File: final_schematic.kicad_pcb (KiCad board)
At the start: 2 copper layers, 54.7 x 60.6 mm, 52 parts, among them J1 Battery Babysitter, J2 BB_SYSOFF, J3 BOOT0, J4 OLED Qwiic, J5 Prog, J8 GPS_COAX, SW1 SW_Push_SESS, SW2 SW_Push_RADIO, SW3 SW_Push_RST, U1 STM32L476VGTx, U2 MTK3339, U3 RFM95W-868S2, U4 BNO055, U5 LT1129-3.3_SO8

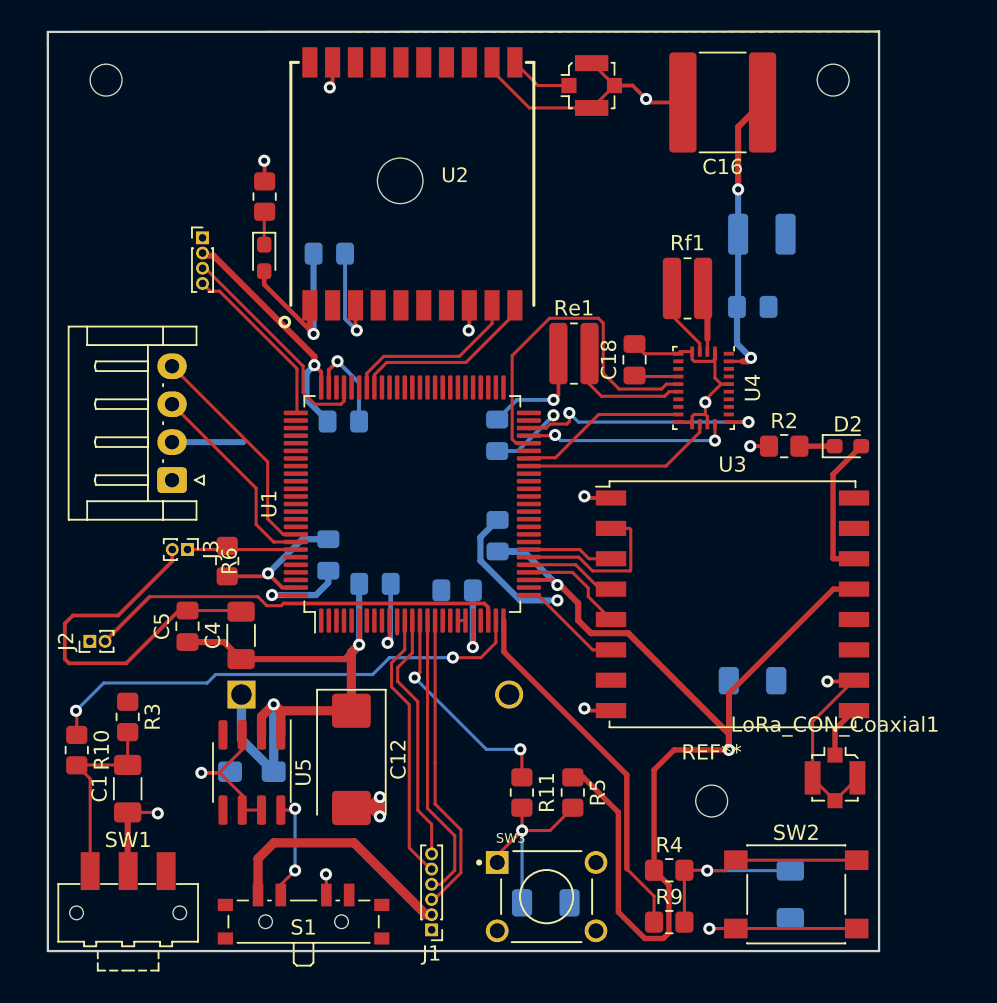
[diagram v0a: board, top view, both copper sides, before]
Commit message: Design Rules Pass, more silkskin
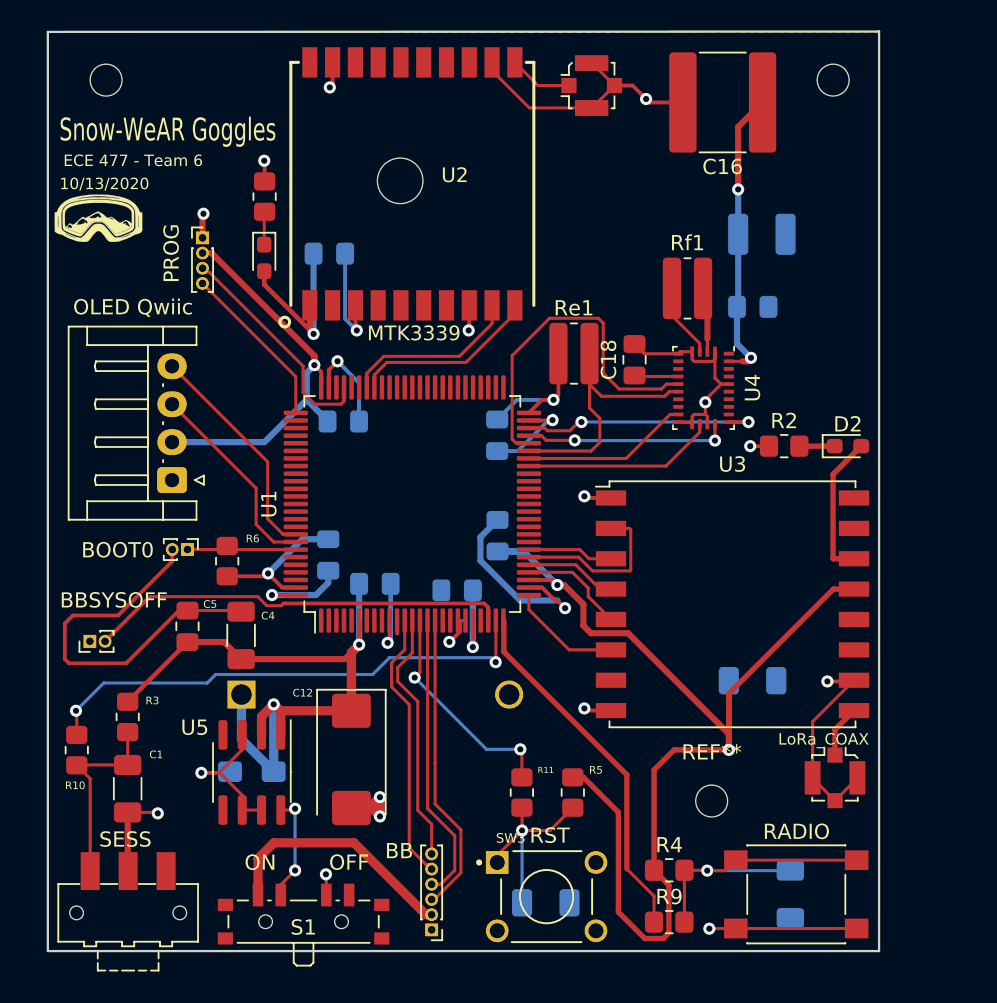
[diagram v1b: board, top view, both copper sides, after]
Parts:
- added G***: LOGO, footprint_lib:logo2, F.Cu at (100.6, 57.7)
- J2: value BB_SYSOFF -> BBSYSOFF
- J5: value Prog -> PROG
- REF**: value MountingHole_2.1mm -> 2.1mm
- renumbered J1 to BB, LoRa_CON_Coaxial1 to LoRa_COAX, SW2 to RADIO, SW1 to SESS
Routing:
- net 3V3: track 201.1 -> 215.1 mm
- net IMU_nRST: track 8.32 -> 19.4 mm
- net GND: track 158.9 -> 166.8 mm, vias 21 -> 23
- net LoRa_RST: track 6.90 -> 8.06 mm
- net session_btn: track 32.6 -> 33.6 mm
- net I2C2_SDA: track 16.8 -> 16.1 mm
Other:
- board text added: "10/13/2020"
- board text added: "BB_CE"
- board text added: "BB_GPOUT"
- board text added: "ECE 477 - Team 6"
- board text added: "I2C3_SCL"
- board text added: "I2C3_SDA"
- board text added: "OFF"
- board text added: "ON"
- board text added: "RST"
- board text added: "Snow-WeAR Goggles"
- board text added: "V_supply"

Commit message: Silkscreen is milkscreen
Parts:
- moved G*** 12.1 mm to (108.2, 48.3)
- renumbered U4 to BNO055, D1 to HEART, U3 to RADIO, D2 to TRANS
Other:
- board text added: "+"
- board text added: "-"
- board text added: "3V3"
- board text added: "BOOT0"
- board text added: "Brought to you by, Mitchell Ciupak Carrie Kemmet Kennedy Monaco Peter Sumner"
- board text added: "C3-PAD2"
- board text added: "GND"
- board text added: "GPS_COAX"
- board text added: "I2C1_SCL"
- board text added: "I2C1_SDA"
- board text added: "Icon Legend"
- board text added: "Pin 1"
- board text added: "SWCLK"
- board text added: "SWDIO"
- board text added: "SYSOFF"

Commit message: Cha Cha Cha Changes
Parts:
- removed C4: 1uF, Capacitor_SMD:C_1206_3216Metric_Pad1.33x1.80mm_HandSolder
- removed C5: 0.1uF, Capacitor_SMD:C_0805_2012Metric_Pad1.18x1.45mm_HandSolder
- removed J3: BOOT0, Connector_PinHeader_1.00mm:PinHeader_1x02_P1.00mm_Vertical
- removed R6: 510, Resistor_SMD:R_0805_2012Metric_Pad1.20x1.40mm_HandSolder
- D1: renamed from HEART; value HEART -> LED_HEARTBEAT_R1
- J1: renamed from BB; footprint Connector_PinHeader_1.00mm:PinHeader_1x06_P1.00mm_Vertical -> Connector_PinHeader_2.54mm:PinHeader_1x06_P2.54mm_Vertical
- J2: value BBSYSOFF -> BB_SYSOFF; footprint Connector_PinHeader_1.00mm:PinHeader_1x02_P1.00mm_Vertical -> Connector_PinHeader_2.54mm:PinHeader_1x02_P2.54mm_Vertical
- J5: value PROG -> Programmer; footprint Connector_PinHeader_1.00mm:PinHeader_1x04_P1.00mm_Vertical -> Connector_PinHeader_2.54mm:PinHeader_1x04_P2.54mm_Vertical
- moved J2 6.98 mm to (107.0, 84.9)
- moved J5 2.32 mm to (108.4, 61.1), turned to 270 degrees
- moved J1 0.61 mm to (122.5, 103.9)
- renumbered TRANS to D2, LoRa_COAX to LoRa_CON_Coaxial1, SESS to SW1, RADIO to SW2, RADIO to U3, BNO055 to U4
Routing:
- net GND: track 166.8 -> 145.9 mm, vias 23 -> 26
- net 3V3: track 215.1 -> 198.6 mm
- net SYSOFF: track 27.7 -> 18.5 mm
- net BB_CE: track 16.7 -> 8.38 mm
- net SWCLK: track 11.1 -> 18.5 mm
- net BOOT0: track 7.37 -> 0.00 mm
- net BB_GPOUT: track 17.9 -> 11.2 mm
- net I2C3_SCL: track 19.1 -> 13.2 mm
- net I2C3_SDA: track 20.0 -> 15.9 mm
- net SWDIO: track 15.3 -> 19.2 mm

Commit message: component update
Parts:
- added R12: 10k, Resistor_SMD:R_0805_2012Metric_Pad1.20x1.40mm_HandSolder, F.Cu at (109.3, 71.9)
- added R13: 10k, Resistor_SMD:R_0805_2012Metric_Pad1.20x1.40mm_HandSolder, B.Cu at (133.9, 69.7)
- added R14: 10k, Resistor_SMD:R_0805_2012Metric_Pad1.20x1.40mm_HandSolder, F.Cu at (126.6, 96.0)
- added R6: 10k, Resistor_SMD:R_0805_2012Metric_Pad1.20x1.40mm_HandSolder, F.Cu at (109.3, 69.8)
- added R7: 10k, Resistor_SMD:R_0805_2012Metric_Pad1.20x1.40mm_HandSolder, B.Cu at (136.1, 72.8)
- added R8: 10k, Resistor_SMD:R_0805_2012Metric_Pad1.20x1.40mm_HandSolder, F.Cu at (126.6, 93.4)
- added U6: TC2014-3.3VxCTTR, Package_TO_SOT_SMD:SOT-23-5, B.Cu at (122.3, 72.0)
- J5: footprint Connector_PinHeader_2.54mm:PinHeader_1x04_P2.54mm_Vertical -> Connector_PinHeader_2.54mm:PinHeader_1x05_P2.54mm_Vertical
- moved R9 4.97 mm to (135.9, 99.6), turned to 270 degrees
- moved R11 3.11 mm to (131.3, 96.8)
- moved D1 2.46 mm to (111.2, 57.8)
- moved R5 2.07 mm to (133.4, 96.8)
- moved J5 1.90 mm to (110.2, 61.6)
- moved R1 1.88 mm to (111.2, 54.4), turned to 0 degrees
- moved R4 1.02 mm to (138.1, 99.6), turned to 270 degrees
- moved J4 0.97 mm to (105.4, 75.8)
- moved G*** 0.91 mm to (107.2, 48.3)
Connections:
- C13 pad 1: 3V3 -> GPS_Vin
- J5 pad 2: 3V3 -> NRST
- J5 pad 3: SWDIO -> 3V3
- J5 pad 4: SWCLK -> SWDIO
- U1 pad 21: 3V3 -> GND
- U1 pad 22: Net-(U1-Pad22) -> 3V3
- U1 pad 64: Net-(U1-Pad64) -> LDO_ERR
- U1 pad 65: Net-(U1-Pad65) -> LDO_SHDN
- U1 pad 73: Net-(U1-Pad73) -> 3V3
- U1 pad 94: BOOT0 -> GND
- U2 pad 1: 3V3 -> GPS_Vin
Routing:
- net 3V3: track 198.6 -> 370.4 mm, vias 11 -> 13
- net NRST: track 14.6 -> 65.2 mm, vias 2 -> 3
- net LDO_ERR: track 0.00 -> 17.5 mm, vias 0 -> 1
- net GPS_Vin: track 0.00 -> 16.4 mm, vias 0 -> 1
- net GND: track 145.9 -> 158.4 mm
- net LDO_SHDN: track 0.00 -> 9.19 mm, vias 0 -> 1
- net radio_btn: track 24.0 -> 18.0 mm
- net I2C3_SDA: track 15.9 -> 18.6 mm
- net I2C3_SCL: track 13.2 -> 15.0 mm
- net USART_TX: track 12.3 -> 13.6 mm
- net SWCLK: track 18.5 -> 17.2 mm
- net Net-(D1-Pad1): track 2.17 -> 3.00 mm
- net SWDIO: track 19.2 -> 18.6 mm
- net Net-(C3-Pad2): track 12.5 -> 12.0 mm

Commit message: keepout
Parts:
- moved C13 3.57 mm to (115.8, 63.5)
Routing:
- net GND: track 158.4 -> 150.0 mm, vias 26 -> 27
- net GPS_Vin: track 16.4 -> 12.9 mm
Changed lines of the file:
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@@
     (thickness 1.6)
     (drawings 53)
-    (tracks 608)
+    (tracks 612)
     (zones 0)
     (modules 56)
@@
   )
   (module Capacitor_SMD:C_0805_2012Metric_Pad1.18x1.45mm_HandSolder (layer B.Cu)
-    (at 115.7947 59.9694)
+    (at 115.7732 63.5381)
     (descr "Capacitor SMD 0805 (2012 Metric), square (rectangular) end terminal, IPC_7351 nominal with elongated pad for handsoldering. (Body size source: IPC-SM-782 page 76, https://www.pcb-3d.com/wordpress/wp-content/uploads/ipc-sm-782a_amendment_1_and_2.pdf, https://docs.google.com/spreadsheets/d/1BsfQQcO9C6DZCsRaXUlFlo91Tg2WpOkGARC1WS5S8t0/edit?usp=sharing), generated with kicad-footprint-generator")
     (tags "capacitor handsolder")
@@
   (segment (start 133.0706 50.372001) (end 133.0956 50.372001) (width 0.2032) (layer F.Cu) (net 2))
   (segment (start 126.5096 47.914882) (end 126.5096 47.372) (width 0.2032) (layer F.Cu) (net 2))
-  (segment (start 128.966719 50.372001) (end 126.5096 47.914882) (width 0.2032) (layer F.Cu) (net 2))
-  (segment (start 133.0706 50.372001) (end 128.966719 50.372001) (width 0.2032) (layer F.Cu) (net 2))
   (segment (start 150.5216 104.4088) (end 142.5616 104.4088) (width 0.2032) (layer F.Cu) (net 2))
   (segment (start 147.6166 94.513) (end 149.0916 95.988) (width 0.2032) (layer F.Cu) (net 2))
@@
   (via (at 117.602 65.024) (size 0.8) (drill 0.4) (layers F.Cu B.Cu) (net 2))
   (segment (start 116.8322 64.2542) (end 117.602 65.024) (width 0.254) (layer B.Cu) (net 2))
-  (segment (start 116.8322 59.9694) (end 116.8322 64.2542) (width 0.254) (layer B.Cu) (net 2))
   (segment (start 117.5096 64.9316) (end 117.602 65.024) (width 0.254) (layer F.Cu) (net 2))
   (segment (start 117.5096 63.372) (end 117.5096 64.9316) (width 0.254) (layer F.Cu) (net 2))
@@
   (segment (start 125.2596 84.773) (end 124.4346 85.598) (width 0.254) (layer F.Cu) (net 2))
   (segment (start 125.2596 84.129) (end 125.2596 84.773) (width 0.254) (layer F.Cu) (net 2))
+  (via (at 126.492 48.9966) (size 0.8) (drill 0.4) (layers F.Cu B.Cu) (net 2))
+  (segment (start 126.5096 48.979) (end 126.492 48.9966) (width 0.254) (layer F.Cu) (net 2))
+  (segment (start 126.5096 47.372) (end 126.5096 48.979) (width 0.254) (layer F.Cu) (net 2))
+  (segment (start 116.8107 64.2327) (end 117.602 65.024) (width 0.254) (layer B.Cu) (net 2))
+  (segment (start 116.8107 63.5381) (end 116.8107 64.2327) (width 0.254) (layer B.Cu) (net 2))
   (via (at 107.0356 73.3298) (size 0.8) (drill 0.4) (layers F.Cu B.Cu) (net 5))
   (via (at 120.2055 66.9163) (size 0.8) (drill 0.4) (layers F.Cu B.Cu) (net 128))
@@
   (segment (start 112.5526 90.0688) (end 112.1307 89.6469) (width 0.6096) (layer F.Cu) (net 5))
   (segment (start 117.2464 90.0688) (end 112.5526 90.0688) (width 0.6096) (layer F.Cu) (net 5))
-  (segment (start 114.7572 59.9694) (end 114.7572 65.2526) (width 0.4064) (layer B.Cu) (net 126))
   (segment (start 114.7572 65.2526) (end 114.7572 65.2526) (width 0.4064) (layer B.Cu) (net 126))
   (via (at 114.7572 65.2526) (size 0.8) (drill 0.4) (layers F.Cu B.Cu) (net 126))
@@
   (segment (start 121.1756 70.4546) (end 115.9736 65.2526) (width 0.254) (layer B.Cu) (net 126))
   (segment (start 121.1756 71.0336) (end 121.1756 70.4546) (width 0.254) (layer B.Cu) (net 126))
+  (segment (start 114.7484 65.2438) (end 114.7572 65.2526) (width 0.254) (layer B.Cu) (net 126))
+  (segment (start 114.7357 65.2311) (end 114.7572 65.2526) (width 0.254) (layer B.Cu) (net 126))
+  (segment (start 114.7357 63.5381) (end 114.7357 65.2311) (width 0.254) (layer B.Cu) (net 126))
   (segment (start 120.7596 68.779) (end 120.7596 67.73077) (width 0.2032) (layer F.Cu) (net 127))
   (segment (start 121.77699 66.929) (end 122.301 66.929) (width 0.2032) (layer F.Cu) (net 127))
@@
       )
     )
+  )
+  (zone (net 0) (net_name "") (layer B.Cu) (hatch edge 0.508)
+    (connect_pads (clearance 0.508))
+    (min_thickness 0.254)
+    (keepout (tracks not_allowed) (vias not_allowed) (copperpour not_allowed))
+    (fill (arc_segments 32) (thermal_gap 0.508) (thermal_bridge_width 0.508))
+    (polygon
+      (pts
+        (xy 129.0447 58.5978) (xy 113.4999 58.5978) (xy 113.4999 49.4411) (xy 129.0701 49.4411)
+      )
+    )
+  )
+  (zone (net 0) (net_name "") (layer B.Cu) (hatch edge 0.508)
+    (connect_pads (clearance 0.508))
+    (min_thickness 0.254)
+    (keepout (tracks not_allowed) (vias not_allowed) (copperpour not_allowed))
+    (fill (arc_segments 32) (thermal_gap 0.508) (thermal_bridge_width 0.508))
+    (polygon
+      (pts
+        (xy 129.0955 63.2079) (xy 118.7196 63.2206) (xy 118.7196 58.5978) (xy 129.0955 58.5978)
+      )
+    )
+  )
+  (zone (net 0) (net_name "") (layer B.Cu) (hatch edge 0.508)
+    (connect_pads (clearance 0.508))
+    (min_thickness 0.254)
+    (keepout (tracks not_allowed) (vias not_allowed) (copperpour not_allowed))
+    (fill (arc_segments 32) (thermal_gap 0.508) (thermal_bridge_width 0.508))
+    (polygon
+      (pts
+        (xy 118.7196 62.1284) (xy 113.4999 62.1284) (xy 113.4999 58.5978) (xy 118.7196 58.5978)
+      )
+    )

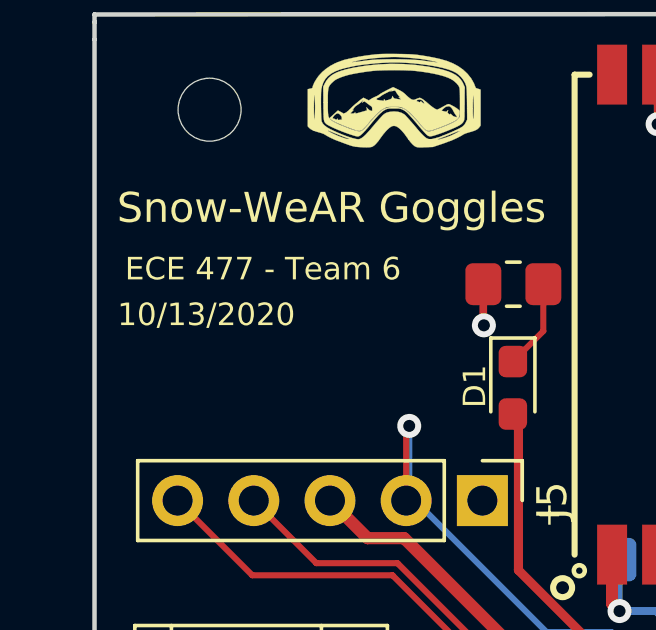
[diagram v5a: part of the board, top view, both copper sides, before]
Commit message: silkscreen changes
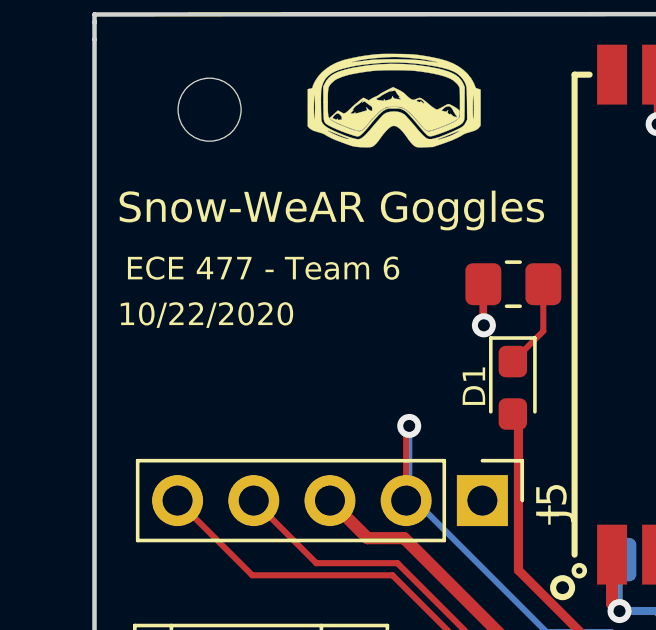
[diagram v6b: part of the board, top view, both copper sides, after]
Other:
- board text added: "10/22/2020"
- board text removed: "10/13/2020"
- board text removed: "BOOT0"
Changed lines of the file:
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@@
   (general
     (thickness 1.6)
-    (drawings 53)
+    (drawings 51)
     (tracks 612)
     (zones 0)
@@
     (tags "capacitor handsolder")
     (attr smd)
-    (fp_text reference C7 (at 0 1.68) (layer B.SilkS)
+    (fp_text reference C7 (at 0.9017 2.2479) (layer B.SilkS)
       (effects (font (size 1 1) (thickness 0.15)) (justify mirror))
     )
@@
     (tags "capacitor handsolder")
     (attr smd)
-    (fp_text reference C9 (at 0 1.68 90) (layer B.SilkS)
+    (fp_text reference C9 (at 0.5246 2.0828 90) (layer B.SilkS)
       (effects (font (size 1 1) (thickness 0.15)) (justify mirror))
     )
@@
     (tags "capacitor handsolder")
     (attr smd)
-    (fp_text reference C15 (at 0 1.68) (layer B.SilkS)
+    (fp_text reference C15 (at -3.8216 0.254) (layer B.SilkS)
       (effects (font (size 1 1) (thickness 0.15)) (justify mirror))
     )
@@
     (tags "capacitor handsolder")
     (attr smd)
-    (fp_text reference C17 (at 0 2.3) (layer B.SilkS)
+    (fp_text reference C17 (at 4.3138 -0.7643) (layer B.SilkS)
       (effects (font (size 1 1) (thickness 0.15)) (justify mirror))
     )
@@
     (tags "capacitor tantalum")
     (attr smd)
-    (fp_text reference C19 (at 0 1.75) (layer B.SilkS)
+    (fp_text reference C19 (at 0.1778 -1.8796) (layer B.SilkS)
       (effects (font (size 1 1) (thickness 0.15)) (justify mirror))
     )
@@
   (module footprint_lib:1N5355BRLG (layer B.Cu)
     (at 110.0074 89.0016)
-    (fp_text reference D3 (at 8.9154 2.8448 180) (layer B.SilkS)
+    (fp_text reference D3 (at 5.3594 -2.8575 180) (layer B.SilkS)
       (effects (font (size 1 1) (thickness 0.15)) (justify mirror))
     )
@@
     (effects (font (size 1 1) (thickness 0.15)) (justify mirror))
   )
-  (gr_text C3-PAD2 (at 125.6284 98.3996) (layer B.SilkS)
+  (gr_text C3-PAD2 (at 119.126 104.902) (layer B.SilkS)
     (effects (font (size 0.5 0.5) (thickness 0.125)) (justify mirror))
   )
@@
     (effects (font (size 0.5 0.5) (thickness 0.125)) (justify mirror))
   )
-  (gr_text BOOT0 (at 106.4768 77.2668 270) (layer B.SilkS)
+  (gr_text SYSOFF (at 109.7915 81.8134 270) (layer B.SilkS)
     (effects (font (size 0.5 0.5) (thickness 0.125)) (justify mirror))
   )
-  (gr_text GND (at 105.3592 77.6732 270) (layer B.SilkS)
+  (gr_text GND (at 107.188 82.5373 270) (layer B.SilkS)
     (effects (font (size 0.5 0.5) (thickness 0.125)) (justify mirror))
   )
-  (gr_text SYSOFF (at 100.9904 83.1088 270) (layer B.SilkS)
+  (gr_text I2C1_SCL (at 101.981 68.326) (layer B.SilkS)
     (effects (font (size 0.5 0.5) (thickness 0.125)) (justify mirror))
   )
-  (gr_text GND (at 99.9744 83.6676 270) (layer B.SilkS)
+  (gr_text I2C1_SDA (at 101.9683 70.9676) (layer B.SilkS)
     (effects (font (size 0.5 0.5) (thickness 0.125)) (justify mirror))
   )
-  (gr_text I2C1_SCL (at 102.2096 67.4624) (layer B.SilkS)
+  (gr_text 3V3 (at 102.8065 73.1393) (layer B.SilkS)
     (effects (font (size 0.5 0.5) (thickness 0.125)) (justify mirror))
   )
-  (gr_text I2C1_SDA (at 102.2096 69.9516) (layer B.SilkS)
+  (gr_text GND (at 102.9208 75.6793) (layer B.SilkS)
     (effects (font (size 0.5 0.5) (thickness 0.125)) (justify mirror))
   )
-  (gr_text 3V3 (at 102.87 72.4408) (layer B.SilkS)
+  (gr_text SWCLK (at 99.9109 64.2747 90) (layer B.SilkS)
     (effects (font (size 0.5 0.5) (thickness 0.125)) (justify mirror))
   )
-  (gr_text GND (at 102.87 74.93) (layer B.SilkS)
+  (gr_text SWDIO (at 102.5271 64.1858 90) (layer B.SilkS)
     (effects (font (size 0.5 0.5) (thickness 0.125)) (justify mirror))
   )
-  (gr_text SWCLK (at 98.2472 63.7032 90) (layer B.SilkS)
+  (gr_text 3V3 (at 105.0163 63.7413 90) (layer B.SilkS)
     (effects (font (size 0.5 0.5) (thickness 0.125)) (justify mirror))
   )
-  (gr_text SWDIO (at 100.6856 63.754 90) (layer B.SilkS)
-    (effects (font (size 0.5 0.5) (thickness 0.125)) (justify mirror))
-  )
-  (gr_text 3V3 (at 102.87 64.3636 90) (layer B.SilkS)
-    (effects (font (size 0.5 0.5) (thickness 0.125)) (justify mirror))
-  )
-  (gr_text GND (at 108.458 63.8556 90) (layer B.SilkS)
+  (gr_text GND (at 110.1852 59.2582 90) (layer B.SilkS)
     (effects (font (size 0.5 0.5) (thickness 0.125)) (justify mirror))
   )
@@
     (effects (font (size 1 1) (thickness 0.25)))
   )
-  (gr_text V_supply (at 119.888 103.124) (layer B.SilkS)
+  (gr_text V_supply (at 119.3165 101.2444) (layer B.SilkS)
     (effects (font (size 0.5 0.5) (thickness 0.125)) (justify mirror))
   )
-  (gr_text I2C3_SDA (at 119.888 102.362) (layer B.SilkS)
+  (gr_text I2C3_SDA (at 125.6792 98.2218) (layer B.SilkS)
     (effects (font (size 0.5 0.5) (thickness 0.125)) (justify mirror))
   )
-  (gr_text I2C3_SCL (at 119.888 101.6) (layer B.SilkS)
+  (gr_text I2C3_SCL (at 125.8189 96.139) (layer B.SilkS)
     (effects (font (size 0.5 0.5) (thickness 0.125)) (justify mirror))
   )
-  (gr_text BB_GPOUT (at 119.634 100.838) (layer B.SilkS)
+  (gr_text BB_GPOUT (at 119.1133 93.7768) (layer B.SilkS)
     (effects (font (size 0.5 0.5) (thickness 0.125)) (justify mirror))
   )
-  (gr_text BB_CE (at 120.396 100.076) (layer B.SilkS)
+  (gr_text BB_CE (at 119.7483 91.5924) (layer B.SilkS)
     (effects (font (size 0.5 0.5) (thickness 0.125)) (justify mirror))
   )
-  (gr_text 10/13/2020 (at 100.981893 55.372) (layer F.SilkS)
+  (gr_text 10/22/2020 (at 100.981893 55.372) (layer F.SilkS)
     (effects (font (size 0.75 0.75) (thickness 0.1875)))
   )
